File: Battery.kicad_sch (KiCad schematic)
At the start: 8 parts, among them J10 1824543, J11 1824527, J12 1824527, J13 1824527

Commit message: v1 done
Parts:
- removed D4, D5: 10V, Diode_SMD:D_SOD-123F, symbol Device:D_Zener
- J10: footprint Argus-Connectors:1824543 -> 1824543; symbol MainBoard:1824543 -> Argus-Connectors:1824543

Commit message: Updated connector locations and types
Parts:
- J10: footprint 1824543 -> Argus-Connectors:1823654
- J11, J12, J13: footprint Argus-Connectors:1824527 -> Argus-Connectors:1823638
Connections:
- net GND: now also J12.3 (MP), J12.4 (MP), J13.3 (MP), J13.4 (MP)
- net GNDREF: no longer J12.3 (MP), J12.4 (MP), J13.3 (MP), J13.4 (MP)
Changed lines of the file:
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@@
-	(symbol
-		(lib_id "power:GNDREF")
-		(at 186.69 119.38 0)
-		(unit 1)
-		(exclude_from_sim no)
-		(in_bom yes)
-		(on_board yes)
-		(dnp no)
-		(property "Reference" "#PWR0117"
-			(at 186.69 125.73 0)
-			(effects
-				(font
-					(size 1.27 1.27)
-				)
-				(hide yes)
-			)
-		)
-		(property "Value" "GNDREF"
-			(at 186.69 123.444 0)
-			(effects
-				(font
-					(size 1.27 1.27)
-				)
-			)
-		)
-		(property "Footprint" ""
-			(at 186.69 119.38 0)
-			(effects
-				(font
-					(size 1.27 1.27)
-				)
-				(hide yes)
-			)
-		)
-		(property "Datasheet" ""
-			(at 186.69 119.38 0)
-			(effects
-				(font
-					(size 1.27 1.27)
-				)
-				(hide yes)
-			)
-		)
-		(property "Description" "Power symbol creates a global label with name \"GNDREF\" , reference supply ground"
-			(at 186.69 119.38 0)
-			(effects
-				(font
-					(size 1.27 1.27)
-				)
-				(hide yes)
-			)
-		)
-		(pin "1"
-		)
-		(instances
-			(project "Avionics-MainBoard"
-				(path "/4c932743-8c6f-426e-9c1f-5a3f2b32c70d/9c9d9468-b4b2-4446-8643-65a41782778e"
-					(reference "#PWR0117")
-					(unit 1)
-				)
-			)
-		)
-	)
 	(symbol
 		(lib_id "power:GNDREF")
@@
 			)
 		)
-		(property "Footprint" "Argus-Connectors:1824527"
+		(property "Footprint" "Argus-Connectors:1823638"
 			(at 124.46 209.22 0)
 			(effects
@@
 			)
 		)
-		(property "Footprint" "1824543"
+		(property "Footprint" "Argus-Connectors:1823654"
 			(at 111.76 162.23 0)
 			(effects
@@
 			)
 		)
-		(property "Footprint" "Argus-Connectors:1824527"
+		(property "Footprint" "Argus-Connectors:1823638"
 			(at 77.8 110.49 0)
 			(effects
@@
 	)
 	(symbol
+		(lib_id "power:GND")
+		(at 186.69 119.38 0)
+		(unit 1)
+		(exclude_from_sim no)
+		(in_bom yes)
+		(on_board yes)
+		(dnp no)
+		(property "Reference" "#PWR0117"
+			(at 186.69 125.73 0)
+			(effects
+				(font
+					(size 1.27 1.27)
+				)
+				(hide yes)
+			)
+		)
+		(property "Value" "GND"
+			(at 186.69 122.936 0)
+			(effects
+				(font
+					(size 1.27 1.27)
+				)
+			)
+		)
+		(property "Footprint" ""
+			(at 186.69 119.38 0)
+			(effects
+				(font
+					(size 1.27 1.27)
+				)
+				(hide yes)
+			)
+		)
+		(property "Datasheet" ""
+			(at 186.69 119.38 0)
+			(effects
+				(font
+					(size 1.27 1.27)
+				)
+				(hide yes)
+			)
+		)
+		(property "Description" "Power symbol creates a global label with name \"GND\" , ground"
+			(at 186.69 119.38 0)
+			(effects
+				(font
+					(size 1.27 1.27)
+				)
+				(hide yes)
+			)
+		)
+		(pin "1"
+		)
+		(instances
+			(project "Avionics-MainBoard"
+				(path "/4c932743-8c6f-426e-9c1f-5a3f2b32c70d/9c9d9468-b4b2-4446-8643-65a41782778e"
+					(reference "#PWR0117")
+					(unit 1)
+				)
+			)
+		)
+	)
+	(symbol
 		(lib_id "MainBoard:1824527")
 		(at 153.67 93.98 270)
@@
 			)
 		)
-		(property "Footprint" "Argus-Connectors:1824527"
+		(property "Footprint" "Argus-Connectors:1823638"
 			(at 58.75 110.49 0)
 			(effects

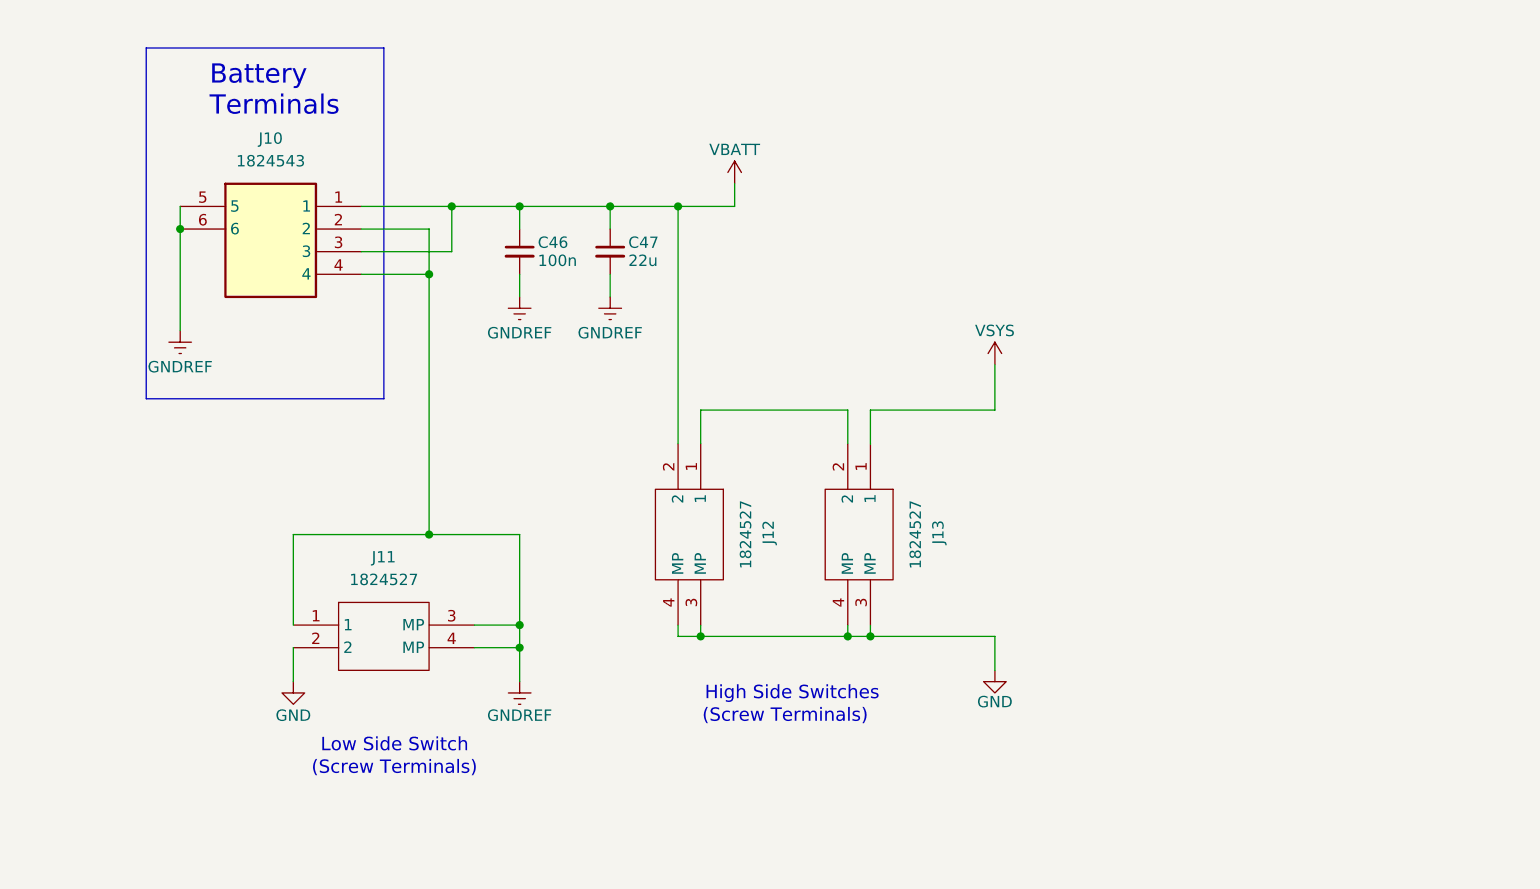
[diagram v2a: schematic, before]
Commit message: Added better protection to SD card, Jetson IO, and added address breakouts to power monitors
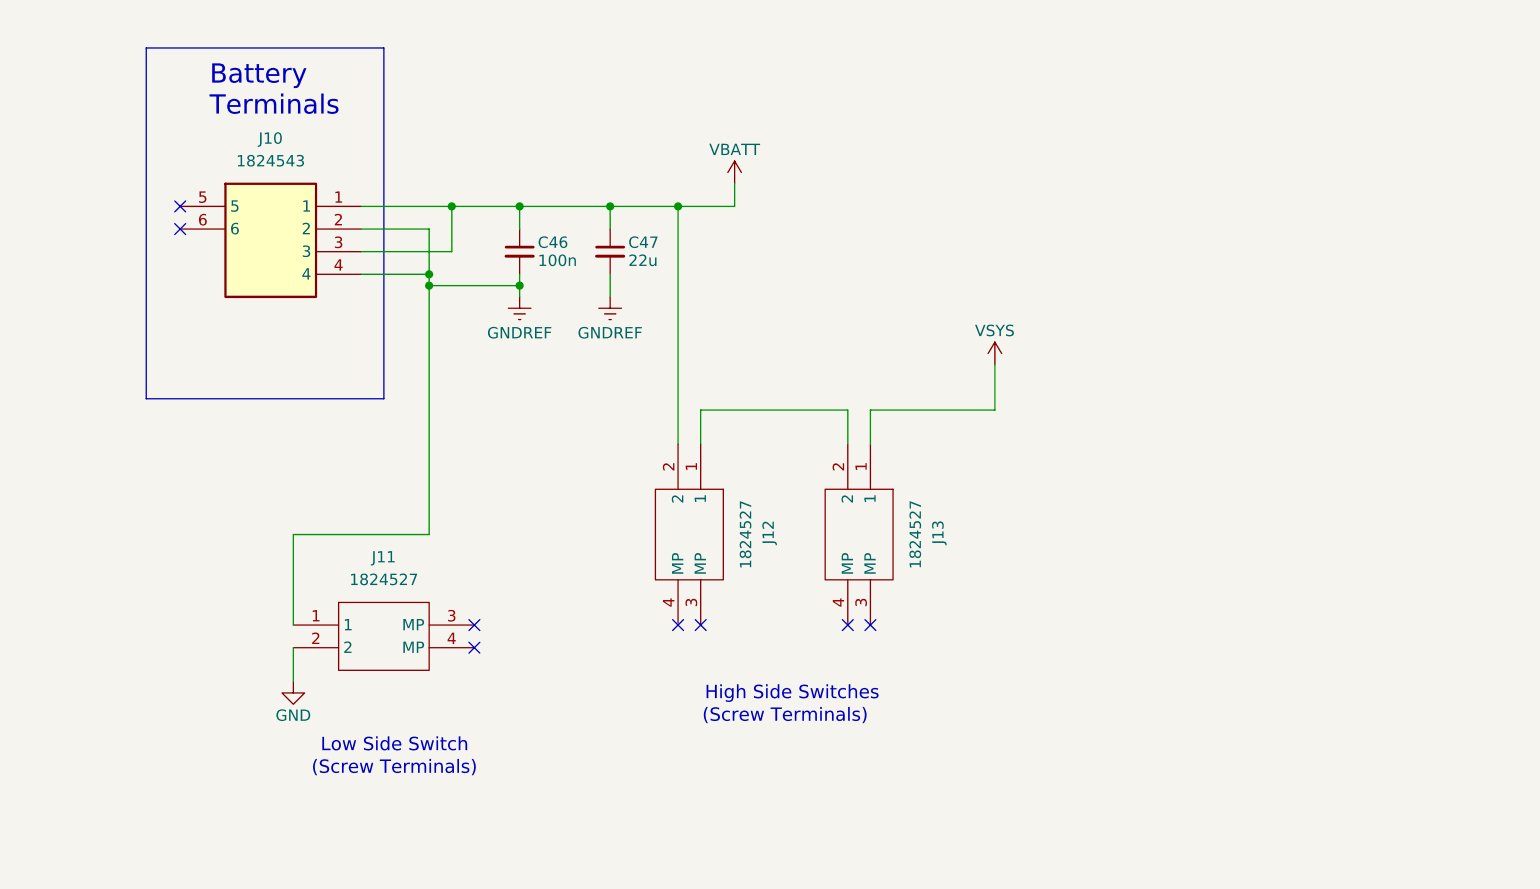
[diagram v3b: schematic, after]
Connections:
- net GND: no longer J12.3 (MP), J12.4 (MP), J13.3 (MP), J13.4 (MP)
- net GNDREF: no longer J10.5, J10.6, J11.3 (MP), J11.4 (MP)
- no-connect marks 0 -> 8

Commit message: Updated version to v2.1
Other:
- company: (none) -> Carnegie Mellon University
- title: (none) -> Argus Mainboard
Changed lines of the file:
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@@
 	(generator_version "8.0")
 	(paper "A4")
+	(title_block
+		(title "Argus Mainboard")
+		(date "2024-11-19")
+		(rev "v2.1")
+		(company "Carnegie Mellon University")
+		(comment 1 "M. Holliday")
+		(comment 2 "N. Khera")
+		(comment 3 "V. Rajesh")
+	)
 	(junction
 		(at 133.35 67.31)

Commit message: v3 partial schematic updates
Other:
- note added: "TODO: Get rid of entirely?"
- moved on the sheet: C46, C47, J10, J11, J12, J13

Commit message: v3 Layout complete
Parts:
- removed J10: 1824543, Argus-Connectors:1823654, symbol Argus-Connectors:1824543
- removed J11, J12, J13: 1824527, Argus-Connectors:1823638, symbol MainBoard:1824527
- added D14: 10V, Diode_SMD:D_SMA, symbol Device:D_Zener_Small
- added J14: 282834-4, Argus-Connectors:TE_282834-4, symbol Connector_Generic:Conn_01x04
- added J16, J17: 282834-2, Argus-Connectors:TE_282834-2, symbol Connector_Generic:Conn_01x02
- C84: renamed from C46; value 100n -> 22u; footprint Capacitor_SMD:C_0603_1608Metric -> Capacitor_SMD:C_1210_3225Metric
- C85: renamed from C47; footprint Capacitor_SMD:C_0603_1608Metric -> Capacitor_SMD:C_1210_3225Metric
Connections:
- net GND: now also D14.2 (A), J17.2 (Pin_2)
- net GNDREF: now also J14.2 (Pin_2), J14.4 (Pin_4), J17.1 (Pin_1)
- net VBATT: now also J14.1 (Pin_1), J14.3 (Pin_3), J16.2 (Pin_2)
- net VSYS: now also D14.1 (K), J16.1 (Pin_1)
- no-connect marks 8 -> 0
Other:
- note added: "High Side Switch"
- note removed: "High Side Switches"
- note removed: "TODO: Get rid of entirely?"

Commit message: v4.0 Updates
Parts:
- added J21: 205338-0004, Connector_Molex:Molex_Pico-Lock_205338-0004_1x04-1MP_P2.00mm_Horizontal, symbol Connector_Generic_MountingPin:Conn_01x04_MountingPin
- added J22, J24, J26: 205338-0002, Connector_Molex:Molex_Pico-Lock_205338-0002_1x02-1MP_P2.00mm_Horizontal, symbol Connector_Generic_MountingPin:Conn_01x02_MountingPin
- added J27: 282834-2, Argus-Connectors:TE_282834-2, symbol Connector_Generic:Conn_01x02
- D14: value 10V -> SMAJ9.0AHR3G; Part SMAJ9.0AHR3G -> 10V
- J20: renamed from J14; now not fitted
- J23: renamed from J17; now not fitted
- J25: renamed from J16; now not fitted
- renumbered C84 to C79, C85 to C80
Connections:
- net GND: now also J21.MP (MountPin), J22.2 (Pin_2), J22.MP (MountPin), J24.MP (MountPin), J26.MP (MountPin)
- net VBATT: now also J26.1 (Pin_1), J27.1 (Pin_1); no longer C79.1, C80.1, J20.1 (Pin_1), J20.3 (Pin_3), J25.2 (Pin_2)
- net GNDREF renamed SYSTEM_VSS
- net SYSTEM_VSS: now also J20.3 (Pin_3), J21.3 (Pin_3), J21.4 (Pin_4), J22.1 (Pin_1); no longer J20.2 (Pin_2)
- net VSYS renamed VCHRG
- net VCHRG: now also J24.1 (Pin_1), J26.2 (Pin_2), J27.2 (Pin_2)
- new net SYSTEM_VDD: C79.1, C80.1, J20.1 (Pin_1), J20.2 (Pin_2), J21.1 (Pin_1), J21.2 (Pin_2), J24.2 (Pin_2), J25.2 (Pin_2)
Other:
- note added: "High Side Switch 1"
- note added: "High Side Switch 2"
- note added: "TODO: CLEANUP"
- note removed: "(Screw Terminals)"
- note removed: "High Side Switch"
- moved on the sheet: C79, C80, D14

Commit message: DFM updates
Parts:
- C79, C80: MPN (none) -> C2803395
- J20, J23, J25, J27: now left out of the parts list
- J21: MPN (none) -> C916325
- J22, J24, J26: MPN (none) -> C17575002
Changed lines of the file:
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@@
+			)
+		)
+		(property "MPN" "C17575002"
+			(at 229.87 81.28 90)
+			(effects
+				(font
+					(size 1.27 1.27)
+				)
+				(hide yes)
 			)
 		)
@@
 		(unit 1)
 		(exclude_from_sim no)
-		(in_bom yes)
+		(in_bom no)
 		(on_board yes)
 		(dnp yes)
@@
 			)
 		)
+		(property "MPN" "C916325"
+			(at 119.38 91.44 0)
+			(effects
+				(font
+					(size 1.27 1.27)
+				)
+				(hide yes)
+			)
+		)
 		(pin "2"
 		)
@@
 			)
 		)
-		(property "Description" "0.1uF +-10% 50V X7R 0603"
+		(property "Description" ""
+			(at 148.59 92.71 0)
+			(effects
+				(font
+					(size 1.27 1.27)
+				)
+				(hide yes)
+			)
+		)
+		(property "MPN" "C2803395"
 			(at 148.59 92.71 0)
 			(effects
@@
 		(unit 1)
 		(exclude_from_sim no)
-		(in_bom yes)
+		(in_bom no)
 		(on_board yes)
 		(dnp yes)
@@
 		(unit 1)
 		(exclude_from_sim no)
-		(in_bom yes)
+		(in_bom no)
 		(on_board yes)
 		(dnp yes)
@@
 			)
 		)
+		(property "MPN" "C17575002"
+			(at 129.54 115.57 0)
+			(effects
+				(font
+					(size 1.27 1.27)
+				)
+				(hide yes)
+			)
+		)
 		(pin "1"
 		)
@@
 			)
 		)
+		(property "MPN" "C17575002"
+			(at 180.34 81.28 90)
+			(effects
+				(font
+					(size 1.27 1.27)
+				)
+				(hide yes)
+			)
+		)
 		(pin "1"
 		)
@@
 			)
 		)
-		(property "Description" "22uF +-20% 10V X5R"
+		(property "Description" ""
+			(at 158.75 92.71 0)
+			(effects
+				(font
+					(size 1.27 1.27)
+				)
+				(hide yes)
+			)
+		)
+		(property "MPN" "C2803395"
 			(at 158.75 92.71 0)
 			(effects
@@
 		(unit 1)
 		(exclude_from_sim no)
-		(in_bom yes)
+		(in_bom no)
 		(on_board yes)
 		(dnp yes)
